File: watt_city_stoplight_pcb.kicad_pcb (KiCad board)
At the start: 2 copper layers, 39.9 x 41.5 mm, 28 parts, among them J201 USB_C_Receptacle_USB2.0_14P, SW301 Reset, SW302 Boot, SW303 SW, SW401 SW_Wuerth_450301014042, U201 SLLC23T5V2U, U301 ESP32-S3-WROOM-1-N8, U401 AP2112K-3.3

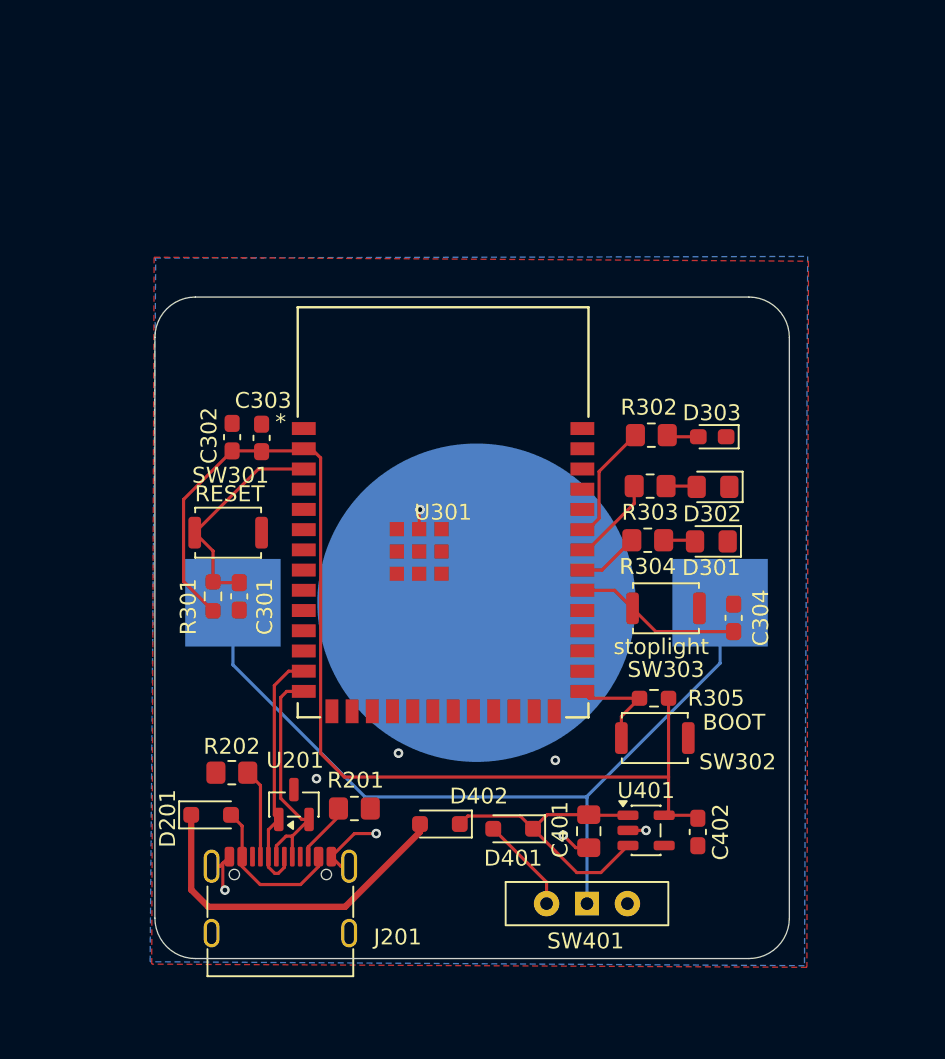
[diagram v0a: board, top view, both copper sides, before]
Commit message: change size
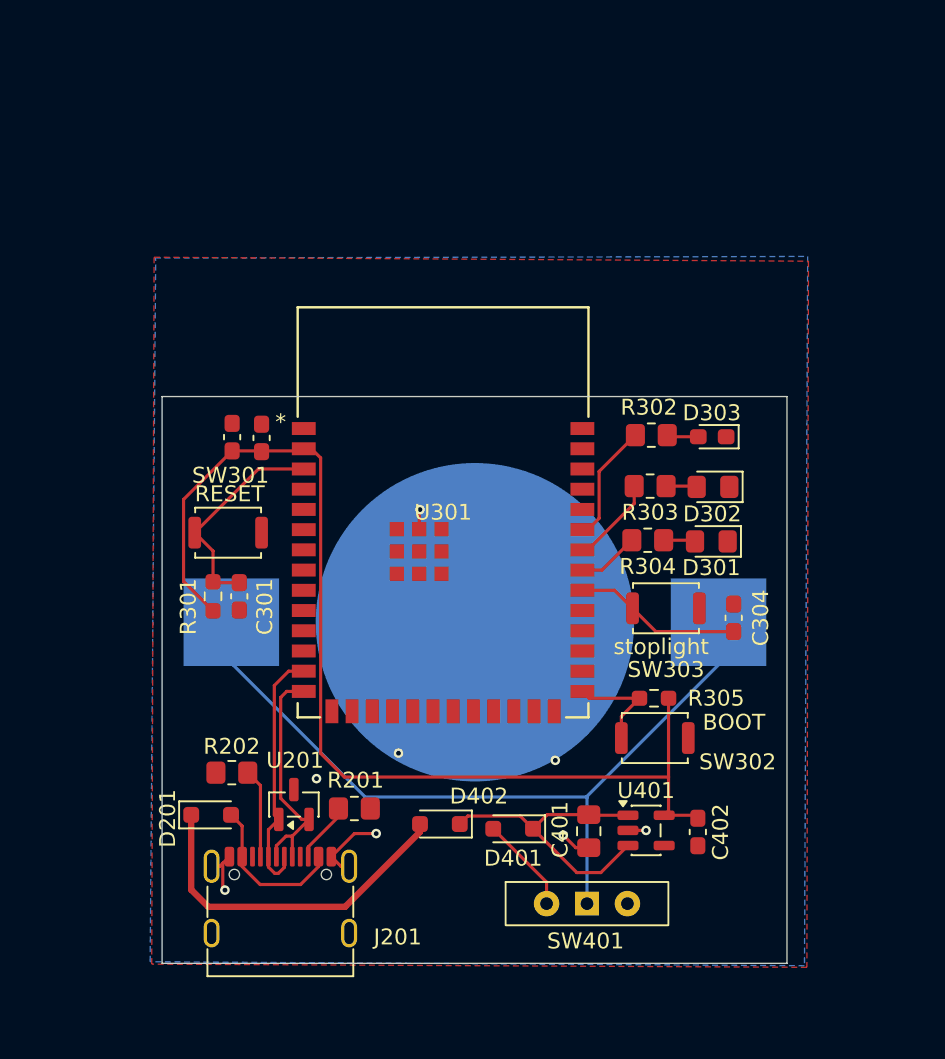
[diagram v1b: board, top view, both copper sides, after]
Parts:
- moved BT401 1.23 mm to (137.1, 92.8)
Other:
- board size 39.9 x 41.5 mm -> 39.2 x 35.6 mm
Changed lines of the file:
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@@
 		(tags "capacitor handsolder")
 		(property "Reference" "C303"
-			(at 2.35 0.1 180)
+			(at 0 1.25 270)
 			(layer "F.SilkS")
+			(hide yes)
 			(effects
 				(font
@@
 			(at 0.1 -1.45 90)
 			(layer "F.SilkS")
+			(hide yes)
 			(effects
 				(font
@@
 	(footprint "Battery:BatteryHolder_Keystone_3008_1x2450"
 		(layer "B.Cu")
-		(at 137.15 91.6 180)
+		(at 137.05 92.825 180)
 		(descr "http://www.keyelco.com/product-pdf.cfm?p=786")
 		(tags "Keystone type 3008 coin cell retainer")
@@
 		)
 	)
-	(gr_arc
-		(start 116.95 74.94)
-		(mid 117.693949 73.143949)
-		(end 119.49 72.4)
-		(stroke
-			(width 0.05)
-			(type default)
-		)
-		(layer "Edge.Cuts")
-	)
-	(gr_line
-		(start 116.95 111.41)
-		(end 116.95 74.94)
-		(stroke
-			(width 0.05)
-			(type default)
-		)
-		(layer "Edge.Cuts")
-	)
-	(gr_line
-		(start 119.49 72.4)
-		(end 154.26 72.4)
-		(stroke
-			(width 0.05)
-			(type default)
-		)
-		(layer "Edge.Cuts")
-	)
-	(gr_arc
-		(start 119.49 113.95)
-		(mid 117.693949 113.206051)
-		(end 116.95 111.41)
-		(stroke
-			(width 0.05)
-			(type default)
-		)
-		(layer "Edge.Cuts")
-	)
-	(gr_arc
-		(start 154.26 72.4)
-		(mid 156.056051 73.143949)
-		(end 156.8 74.94)
-		(stroke
-			(width 0.05)
-			(type default)
-		)
-		(layer "Edge.Cuts")
-	)
-	(gr_line
-		(start 154.26 113.95)
-		(end 119.49 113.95)
-		(stroke
-			(width 0.05)
-			(type default)
-		)
-		(layer "Edge.Cuts")
-	)
-	(gr_line
-		(start 156.8 74.94)
-		(end 156.8 111.41)
-		(stroke
-			(width 0.05)
-			(type default)
-		)
-		(layer "Edge.Cuts")
-	)
-	(gr_arc
-		(start 156.8 111.41)
-		(mid 156.056051 113.206051)
-		(end 154.26 113.95)
+	(gr_rect
+		(start 117.4 78.65)
+		(end 156.65 114.25)
 		(stroke
 			(width 0.05)
 			(type default)
 		)
+		(fill no)
 		(layer "Edge.Cuts")
 	)
@@
 	)
 	(segment
+		(start 148.4125 93.4125)
+		(end 153.3 93.4125)
+		(width 0.2)
+		(layer "F.Cu")
+		(net "Net-(U301-IO39)")
+	)
+	(segment
+		(start 143.8 90.82)
+		(end 145.82 90.82)
+		(width 0.2)
+		(layer "F.Cu")
+		(net "Net-(U301-IO39)")
+	)
+	(segment
+		(start 146.95 91.95)
+		(end 148.4125 93.4125)
+		(width 0.2)
+		(layer "F.Cu")
+		(net "Net-(U301-IO39)")
+	)
+	(segment
+		(start 145.82 90.82)
+		(end 146.95 91.95)
+		(width 0.2)
+		(layer "F.Cu")
+		(net "Net-(U301-IO39)")
+	)
+	(segment
 		(start 145.03 89.55)
 		(end 143.8 89.55)
@@
 		(net "Net-(D302-A)")
 	)
-	(segment
-		(start 148.4125 93.4125)
-		(end 153.3 93.4125)
-		(width 0.2)
-		(layer "F.Cu")
-		(net "Net-(U301-IO39)")
-	)
-	(segment
-		(start 143.8 90.82)
-		(end 145.82 90.82)
-		(width 0.2)
-		(layer "F.Cu")
-		(net "Net-(U301-IO39)")
-	)
-	(segment
-		(start 146.95 91.95)
-		(end 148.4125 93.4125)
-		(width 0.2)
-		(layer "F.Cu")
-		(net "Net-(U301-IO39)")
-	)
-	(segment
-		(start 145.82 90.82)
-		(end 146.95 91.95)
-		(width 0.2)
-		(layer "F.Cu")
-		(net "Net-(U301-IO39)")
-	)
 	(zone

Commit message: updated layout (usb/buttons), generated gerbers
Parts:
- removed SW301: Reset, Button_Switch_SMD:SW_Push_SPST_NO_Alps_SKRK
- removed SW302: Boot, Button_Switch_SMD:SW_Push_SPST_NO_Alps_SKRK
- removed SW303: SW, Button_Switch_SMD:SW_Push_SPST_NO_Alps_SKRK
- added S301: TS-1088-AR02016, TS-1088-AR02016:SW_TS-1088-AR02016, F.Cu at (121.9, 87.3)
- added S302: TS-1088-AR02016, TS-1088-AR02016:SW_TS-1088-AR02016, F.Cu at (149.0, 91.7)
- added S303: TS-1088-AR02016, TS-1088-AR02016:SW_TS-1088-AR02016, F.Cu at (148.4, 100.2)
- J201: value USB_C_Receptacle_USB2.0_14P -> USB4110-GF-A; footprint Connector_USB:USB_C_Receptacle_G-Switch_GT-USB-7010ASV -> USB4110_GF_A:USB4110-GF-A_GCT
- SW401: value SW_Wuerth_450301014042 -> 500SSP1S2M2QEA; footprint Button_Switch_THT:SW_Slide-03_Wuerth-WS-SLTV_10x2.5x6.4_P2.54mm -> 500SSP1S2M2QEA:500SSP1_EWI
- moved D201 8.69 mm to (129.2, 104.3), turned to 180 degrees
- moved R201 8.61 mm to (121.2, 106.9), turned to 0 degrees
- moved R202 8.17 mm to (128.7, 106.7), turned to 180 degrees
- moved SW401 4.63 mm to (139.6, 111.8), turned to 90 degrees
- moved J201 2.28 mm to (126.5, 112.8)
- moved U201 0.83 mm to (124.9, 104.0), turned to -90 degrees
- renumbered C302 to C301, C303 to C302, C301 to C303, R305 to R302, R304 to R303, R303 to R304, R302 to R305
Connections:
- J201 pad A8: (no net) -> unconnected-(J201-SBU1-PadA8)
- J201 pad B8: (no net) -> unconnected-(J201-SBU2-PadB8)
- R201 pad 2: Net-(J201-CC2) -> Net-(J201-CC1)
- R202 pad 2: Net-(J201-CC1) -> Net-(J201-CC2)
- U201 pad 1: /USB_D- -> /USB_D+
- U201 pad 2: /USB_D+ -> /USB_D-
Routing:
- net /power/+5V_USB: track 22.0 -> 3.70 mm
- net /USB_D-: track 16.0 -> 19.1 mm
- net Net-(D201-A): track 9.89 -> 12.5 mm
- net Net-(D401-A): track 6.09 -> 8.49 mm
- net Net-(U301-IO41): track 6.23 -> 5.21 mm
- net Net-(J201-CC1): track 5.61 -> 4.62 mm
- net Net-(BT401-+): track 51.9 -> 51.2 mm
- net GND: track 12.2 -> 11.5 mm, vias 8 -> 12
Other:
- board size 39.2 x 35.6 mm -> 39.2 x 37.3 mm

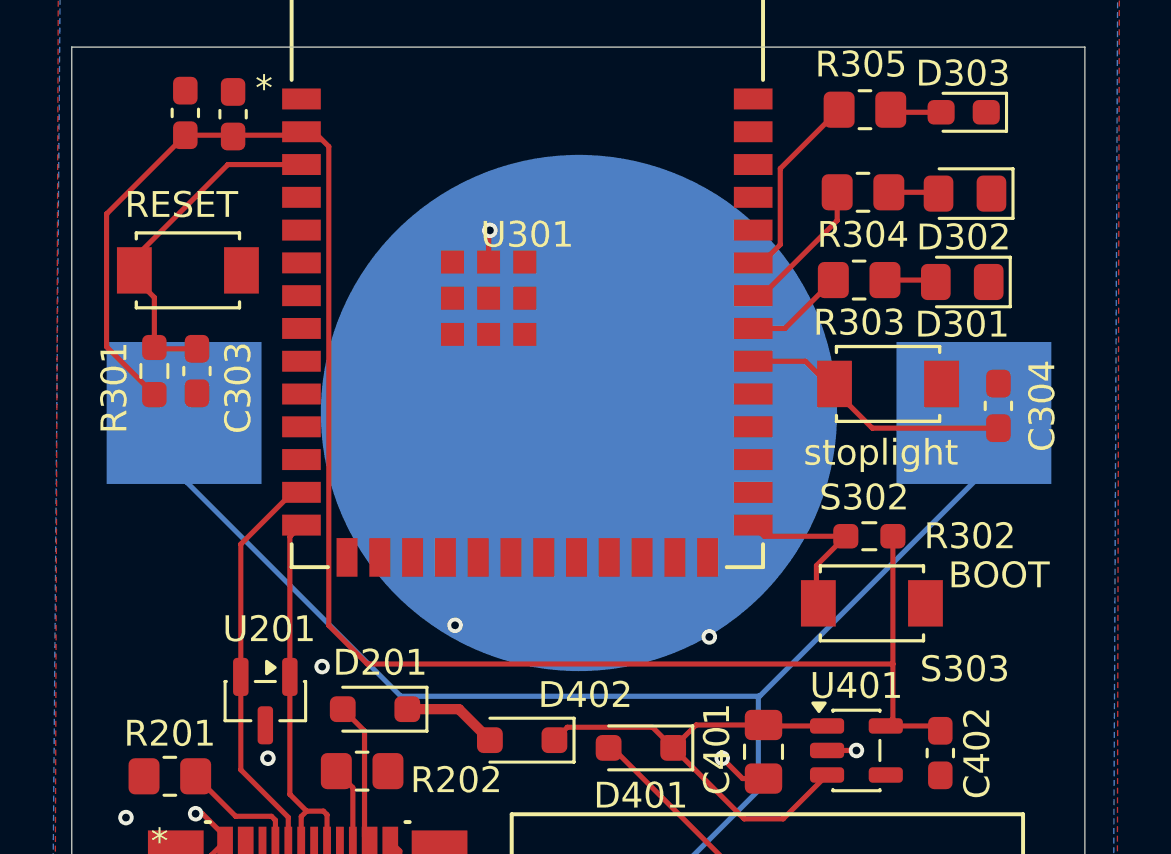
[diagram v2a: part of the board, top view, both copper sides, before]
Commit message: changed coin cell holder
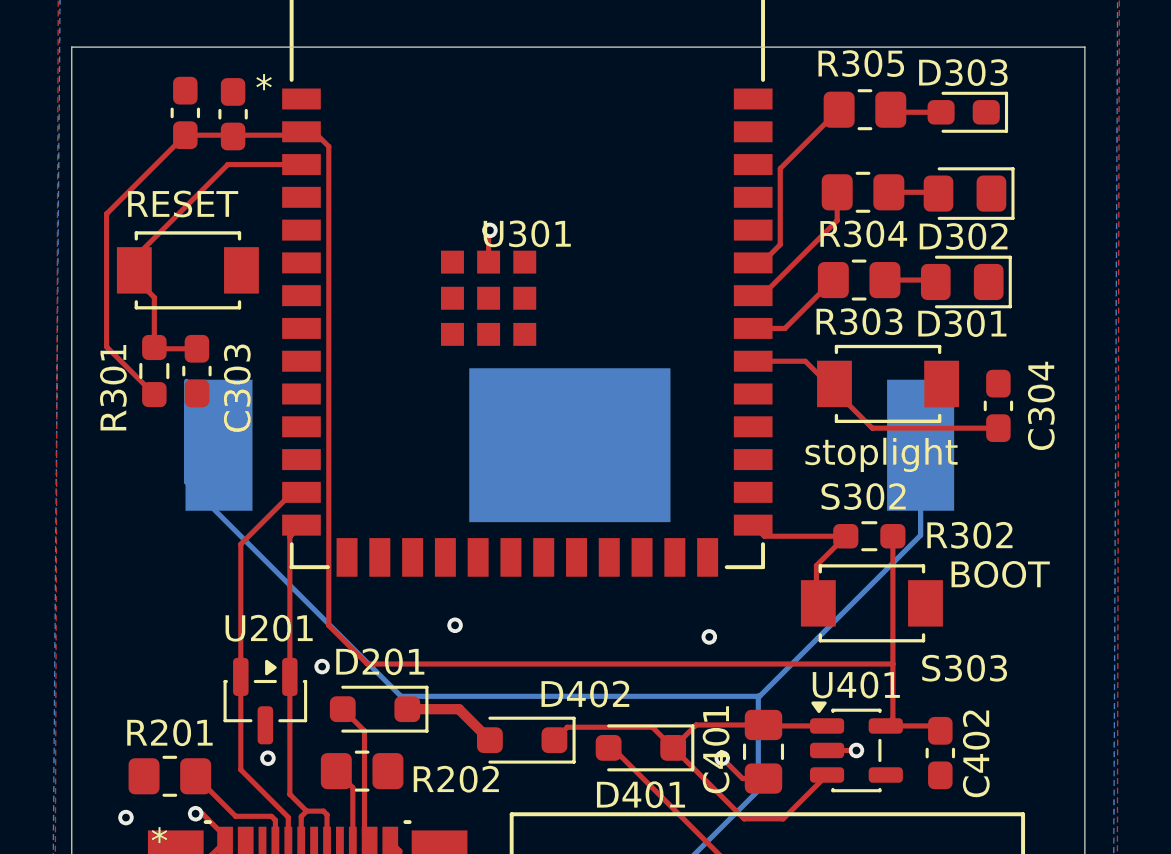
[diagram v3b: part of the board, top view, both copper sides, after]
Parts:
- removed BT401: LIR2450, Battery:BatteryHolder_Keystone_3008_1x2450
- added BT402: BC-2005, BC_2005_TR:BAT_BC-2005, B.Cu at (136.7, 94.1)

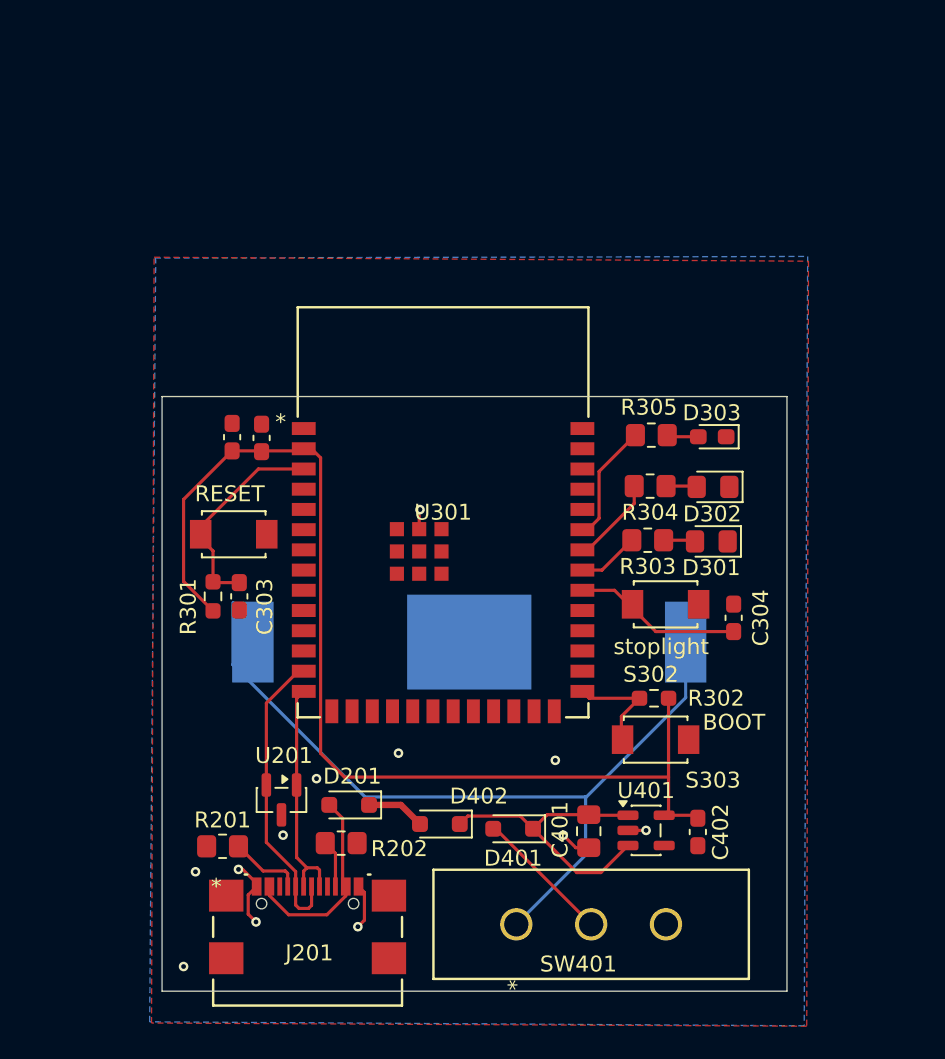
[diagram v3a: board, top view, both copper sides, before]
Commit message: added button pullup + mounting holes
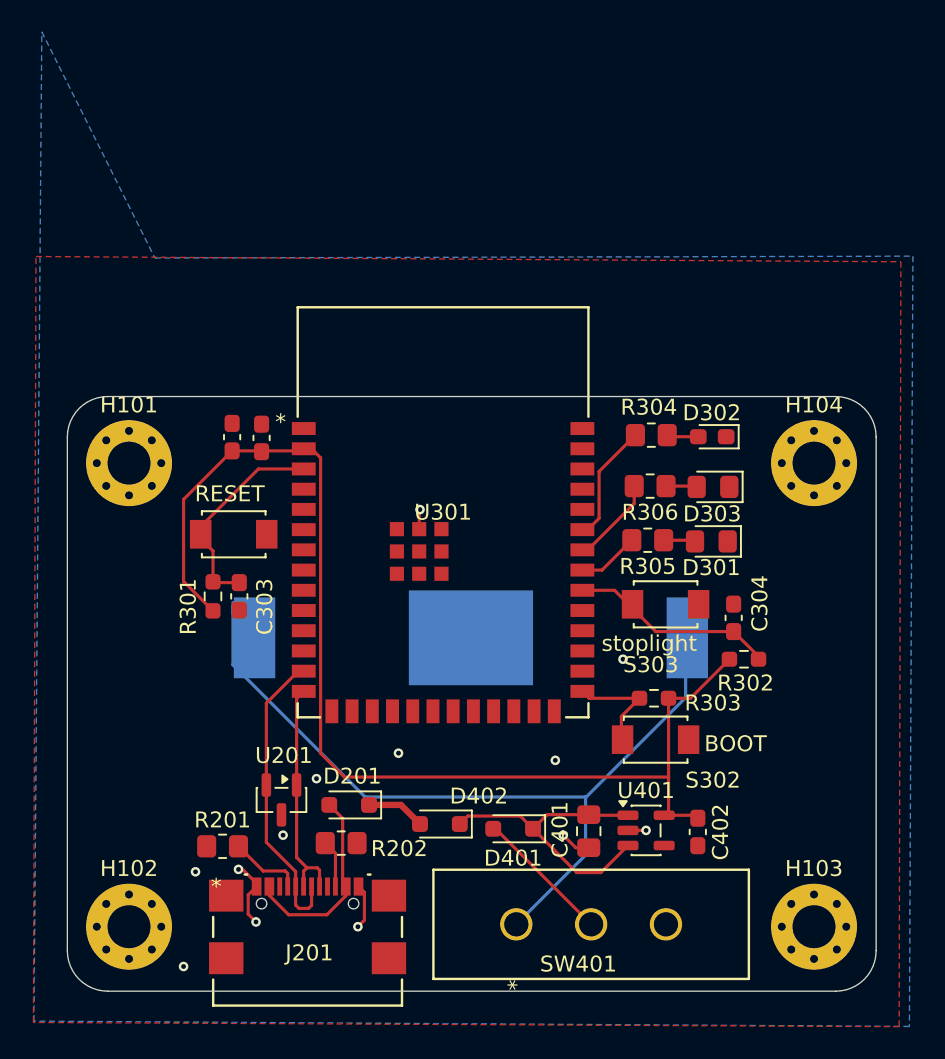
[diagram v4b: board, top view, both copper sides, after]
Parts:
- removed BT402: BC-2005, BC_2005_TR:BAT_BC-2005
- added BT401: BC-2005, BC_2005_TR:BAT_BC-2005, B.Cu at (136.8, 93.8)
- added H101: MountingHole_Pad_MP, MountingHole:MountingHole_2.7mm_M2.5_Pad_Via, F.Cu at (115.3, 82.8)
- added H102: MountingHole_Pad_MP, MountingHole:MountingHole_2.7mm_M2.5_Pad_Via, F.Cu at (115.3, 112.0)
- added H103: MountingHole_Pad_MP, MountingHole:MountingHole_2.7mm_M2.5_Pad_Via, F.Cu at (158.3, 112.0)
- added H104: MountingHole_Pad_MP, MountingHole:MountingHole_2.7mm_M2.5_Pad_Via, F.Cu at (158.3, 82.8)
- added R302: 10k, Resistor_SMD:R_0603_1608Metric_Pad0.98x0.95mm_HandSolder, F.Cu at (153.9, 95.2)
- renumbered D303 to D302, D302 to D303, R302 to R303, R305 to R304, R303 to R305, R304 to R306, S303 to S302, S302 to S303
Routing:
- net /mcu/3V3: track 67.7 -> 72.5 mm
- net Net-(U301-IO39): track 10.6 -> 13.0 mm
- net GND: vias 12 -> 13
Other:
- board size 39.2 x 37.3 mm -> 50.8 x 37.3 mm

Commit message: changed battery
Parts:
- removed BT401: BC-2005, BC_2005_TR:BAT_BC-2005
- added J401: S2B-PH-K-SLFSN, S2B-PH_K_S:CONN_S2B-PH-K-S_JST, B.Cu at (159.2, 102.1)
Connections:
- J201 pad 15: (no net) -> GND
- J201 pad 16: (no net) -> GND
- J201 pad 17: (no net) -> GND
- J201 pad 18: (no net) -> GND
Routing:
- net Net-(J401-Pad1): track 51.6 -> 23.5 mm
- net /USB_D-: track 19.1 -> 18.6 mm
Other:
- board text added: "gnd"
- board text added: "pwr"
